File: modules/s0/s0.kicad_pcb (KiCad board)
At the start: 2 copper layers, 54.6 x 86.4 mm, 61 parts, among them J3 USB_C_Receptacle_USB2.0_14P, J4 BAT_JST_01x02, J5 Conn_Coaxial, J6 Conn_Coaxial, Q1 SS8050, Q2 SS8050, Q3 SS8050, SW1 SW_Push, SW2 SW_Push, U1 TXB0108RGY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

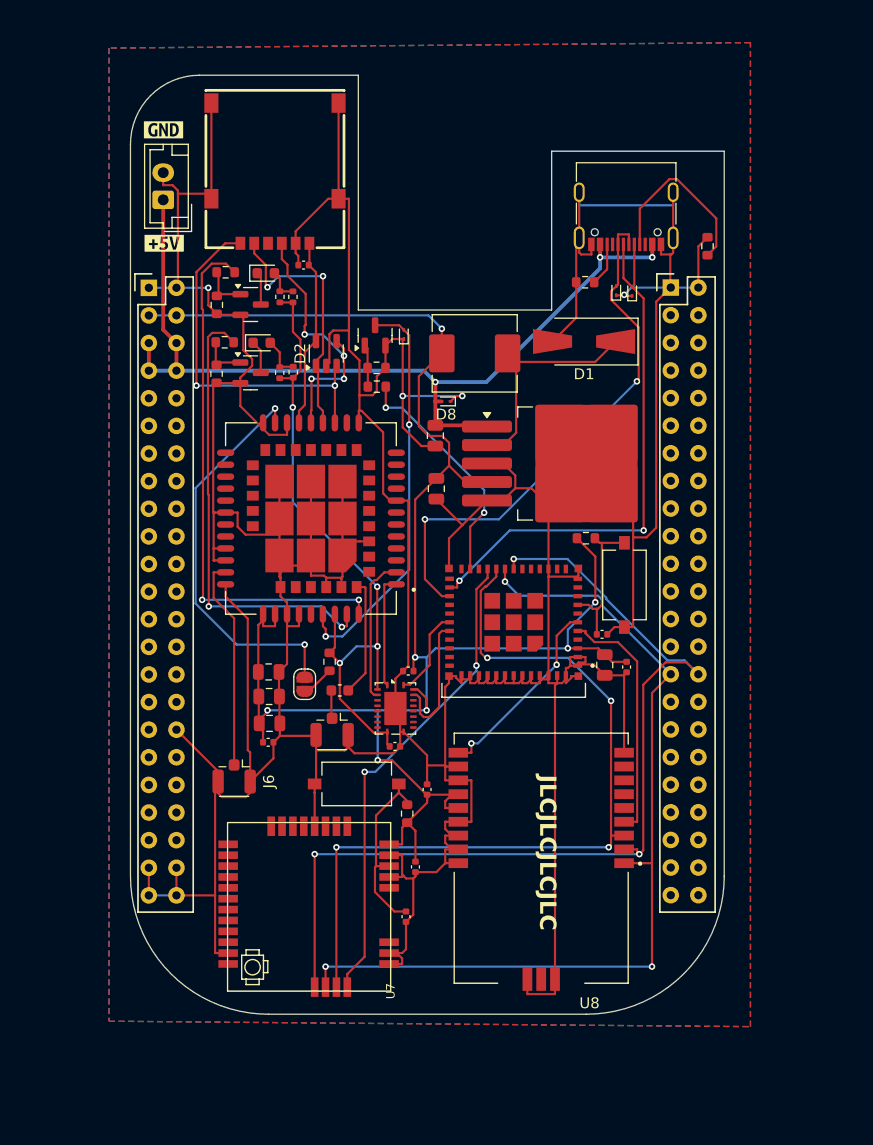
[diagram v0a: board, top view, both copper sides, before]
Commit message: fix: add fuse, ferrite bead and fixes from gpt
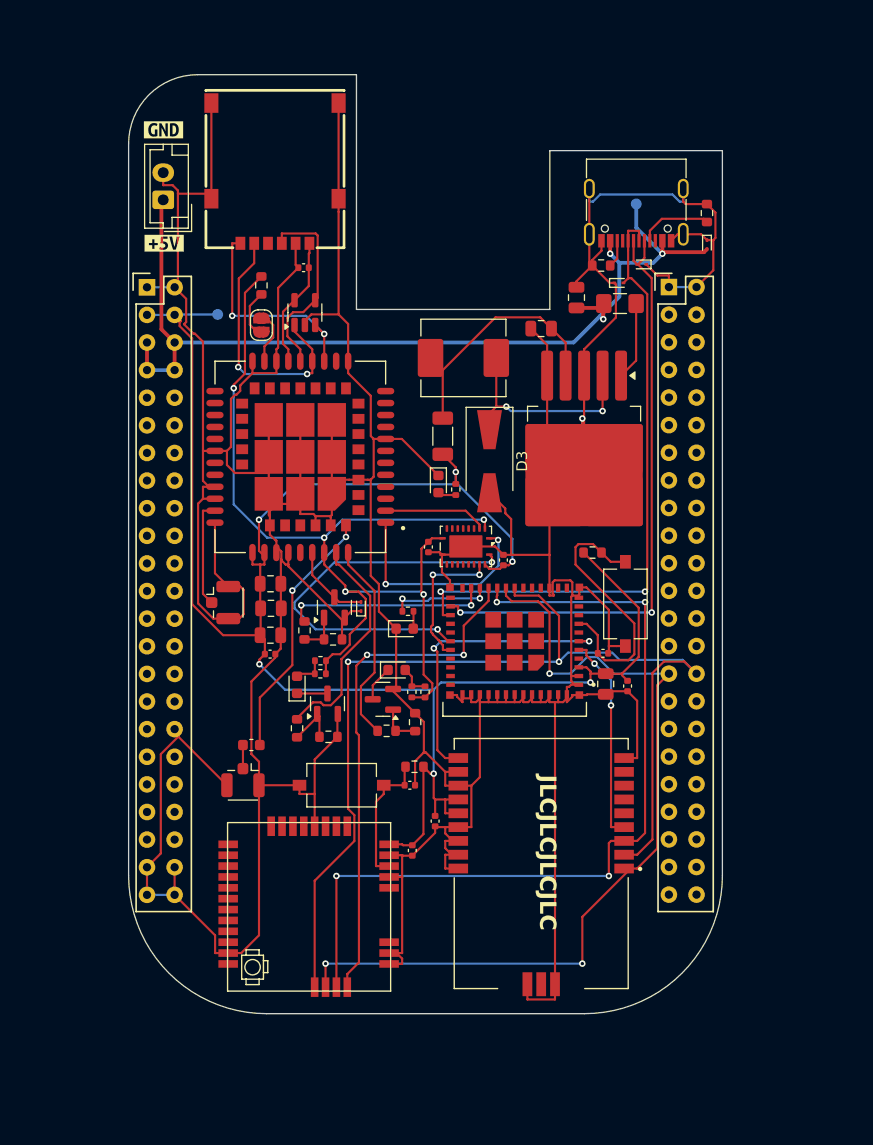
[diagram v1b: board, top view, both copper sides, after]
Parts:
- added D10: LED, LED_SMD:LED_0603_1608Metric, F.Cu at (129.2, 94.9)
- added D9: ESD9B5.0ST5G, Diode_SMD:D_SOD-923, F.Cu at (125.2, 92.9)
- added F1: Fuse, Fuse:Fuse_1206_3216Metric_Pad1.42x1.75mm_HandSolder, F.Cu at (149.0, 65.0)
- added FB1: FerriteBead, Inductor_SMD:L_1206_3216Metric_Pad1.22x1.90mm_HandSolder, F.Cu at (132.7, 77.2)
- added R16: 10K, Resistor_SMD:R_0603_1608Metric, F.Cu at (146.5, 87.9)
- added R17: 10K, Resistor_SMD:R_0603_1608Metric, F.Cu at (130.1, 107.6)
- added TP1: TestPoint, TestPoint:TestPoint_Pad_D1.0mm, B.Cu at (150.5, 55.8)
- added TP2: TestPoint, TestPoint:TestPoint_Pad_D1.0mm, B.Cu at (145.7, 80.9)
- added TP3: TestPoint, TestPoint:TestPoint_Pad_D1.0mm, B.Cu at (112.0, 66.0)
- D1: value 40V 3A 550mV@3A Schottky -> ESD9B5.0ST5G; footprint Diode_SMD:D_SMA-SMB_Universal_Handsoldering -> Diode_SMD:D_SOD-923
- D2: value ESDA6V1SC5 -> ESD9B5.0ST5G; footprint Package_TO_SOT_SMD:SOT-23-5 -> Diode_SMD:D_SOD-923
- D3: value LED -> 40V 3A 550mV@3A Schottky; footprint LED_SMD:LED_0603_1608Metric -> Diode_SMD:D_SMA-SMB_Universal_Handsoldering
- D4: value LED -> ESD9B5.0ST5G; footprint LED_SMD:LED_0603_1608Metric -> Diode_SMD:D_SOD-923
- D5, D7, D8: value ESD9B5.0ST5G -> LED; footprint Diode_SMD:D_SOD-923 -> LED_SMD:LED_0603_1608Metric
- D6: value ESD9B5.0ST5G -> ESDA6V1SC5; footprint Diode_SMD:D_SOD-923 -> Package_TO_SOT_SMD:SOT-23-5
- R10: value 47K -> 100; footprint Resistor_SMD:R_0603_1608Metric -> Resistor_SMD:R_0402_1005Metric
- R12, R8: value 100 -> 47K; footprint Resistor_SMD:R_0402_1005Metric -> Resistor_SMD:R_0603_1608Metric
- R14, R15, R3: value 10K -> 100; footprint Resistor_SMD:R_0603_1608Metric -> Resistor_SMD:R_0402_1005Metric
- R4: value 4.7K -> 10K
- R7: value 47K -> 4.7K
- U1: value TXB0108RGY -> BEAGLEBONEBLACK; footprint Package_DFN_QFN:Texas_RGY_R-PVQFN-N20_EP2.05x3.05mm -> modules:BB_Cape
- U4: value BEAGLEBONEBLACK -> TXB0108RGY; footprint modules:BB_Cape -> Package_DFN_QFN:Texas_RGY_R-PVQFN-N20_EP2.05x3.05mm
- moved D7 47.5 mm to (119.3, 100.1)
- moved R6 42.5 mm to (119.3, 104.1), turned to 90 degrees
- moved R11 41.0 mm to (122.2, 104.8), turned to 180 degrees
- moved Q3 38.3 mm to (127.2, 101.4), turned to 180 degrees
- moved D2 36.4 mm to (157.0, 59.6), turned to -90 degrees
- moved R10 35.0 mm to (131.1, 100.7), turned to -90 degrees
- moved R13 34.9 mm to (121.4, 99.0), turned to 0 degrees
- moved D4 34.6 mm to (151.0, 61.4), turned to 180 degrees
- moved R12 34.1 mm to (130.2, 103.5)
- moved R9 33.6 mm to (121.5, 97.8), turned to 0 degrees
- moved R7 33.4 mm to (127.5, 104.3)
- moved JP1 33.3 mm to (116.0, 67.0)
- moved Q2 31.2 mm to (122.1, 101.8), turned to 90 degrees
- moved D6 28.7 mm to (120.0, 65.8)
- moved R5 27.5 mm to (120.0, 95.1), turned to 90 degrees
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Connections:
- C2 pad 1: +3V3 -> Net-(U2-FB)
- D1 pad 1: Net-(D1-K) -> GND
- D1 pad 2: GND -> USB_D+
- D2 pad 1: SIM_CLK -> GND
- D2 pad 2: GND -> +5V
- D3 pad 2: Net-(D3-A) -> GND
- D4 pad 1: Net-(D4-K) -> GND
- D4 pad 2: Net-(D4-A) -> USB_D-
- D5 pad 2: PWR_KEY -> Net-(D5-A)
- D6 pad 1: GND -> SIM_CLK
- D6 pad 2: USB_D+ -> GND
- D7 pad 1: GND -> Net-(D7-K)
- D7 pad 2: USB_D- -> Net-(D7-A)
- D8 pad 1: GND -> Net-(D8-K)
- D8 pad 2: +5V -> Net-(D8-A)
- L1 pad 1: Net-(D1-K) -> Net-(D3-K)
- L1 pad 2: +3V3 -> Net-(U2-FB)
- Q2 pad 3: Net-(D3-K) -> Net-(D7-K)
- Q3 pad 3: Net-(D4-K) -> Net-(D8-K)
- R10 pad 1: GND -> Net-(D8-A)
- R10 pad 2: Net-(Q2-B) -> +1V8
- R11 pad 2: Net-(Q3-B) -> Net-(Q2-B)
- R12 pad 1: Net-(D3-A) -> GND
- R12 pad 2: +1V8 -> Net-(Q3-B)
- R13 pad 1: Net-(D4-A) -> Net-(D7-A)
- R14 pad 1: +3V3 -> Net-(D8-A)
- R14 pad 2: MCU_RST -> +1V8
- R15 pad 1: +3V3 -> Net-(D10-A)
- R15 pad 2: LORA_RST -> LED
- R3 pad 1: +1V8 -> Net-(D5-A)
- R3 pad 2: Net-(JP1-A) -> +3V3
- R4 pad 1: Net-(Q1-B) -> +1V8
- R4 pad 2: SIM7080G_PWR -> Net-(JP1-A)
- R5 pad 1: Net-(Q2-B) -> Net-(Q1-B)
- R5 pad 2: NETLIGHT -> SIM7080G_PWR
- R6 pad 1: Net-(Q3-B) -> Net-(Q2-B)
- R6 pad 2: STATUS -> NETLIGHT
- R7 pad 1: GND -> Net-(Q3-B)
- R7 pad 2: Net-(Q1-B) -> STATUS
- R8 pad 1: Net-(D3-A) -> GND
- R8 pad 2: +1V8 -> Net-(Q1-B)
- R9 pad 1: Net-(D4-A) -> Net-(D7-A)
- U2 pad 1: +5V -> Net-(U2-VIN)
- U2 pad 2: Net-(D1-K) -> Net-(D3-K)
- U2 pad 4: +3V3 -> Net-(U2-FB)
- U6 pad 22: unconnected-(U6-IO8-Pad22) -> LED
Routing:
- net Net-(JP1-B): track 36.9 -> 5.02 mm, vias 2 -> 0
- net STATUS: track 49.5 -> 18.6 mm, vias 2 -> 0
- net PWR_KEY: track 37.5 -> 7.58 mm, vias 2 -> 0
- net SIM7080G_TXD: track 8.27 -> 36.7 mm, vias 0 -> 2
- net +1V8: track 61.4 -> 89.8 mm, vias 4 -> 5
- net Net-(U2-FB): track 0.00 -> 23.3 mm
- net NETLIGHT: track 42.3 -> 20.9 mm, vias 2 -> 0
- net Net-(D1-K): track 20.7 -> 0.00 mm
- net Net-(D3-K): track 3.05 -> 20.1 mm, vias 0 -> 2
- net SIM_DATA: track 33.6 -> 20.3 mm
- net GNSS_ANT: track 10.9 -> 23.5 mm, vias 0 -> 2
- net MCU_RST: track 13.5 -> 25.2 mm
- net Net-(J3-CC1): track 16.7 -> 6.75 mm
- net MOSI: track 88.3 -> 98.1 mm, vias 3 -> 2
- net RF_ANT: track 19.6 -> 9.88 mm
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- removed copper zone on B.Cu, net GND
- removed copper zone on F.Cu, net GND
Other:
- outline, holes or cut-outs redrawn
- board text added: "https://abstractmachines.fr"
- board text removed: "https://github.com/absmach/s0"

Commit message: fix: add logo name of the board on silkscreen
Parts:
- moved G*** 3.14 mm to (131.5, 109.5)
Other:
- board text added: "S0 IoT Gateway"
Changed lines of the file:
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@@
 	(footprint "LOGO"
 		(layer "B.Cu")
-		(at 132 112.6 180)
+		(at 131.5 109.5 180)
 		(property "Reference" "G***"
 			(at 0 0 0)
@@
 		)
 	)
-	(gr_text "https://abstractmachines.fr"
-		(at 147.4 128.1 0)
+	(gr_text "S0 IoT Gateway"
+		(at 139.763616 128 0)
 		(layer "B.SilkS")
 		(effects
+			(font
+				(size 1.5 1.5)
+				(thickness 0.2)
+			)
+			(justify left bottom mirror)
+		)
+	)
+	(gr_text "https://abstractmachines.fr"
+		(at 146.942189 124.772838 0)
+		(layer "B.SilkS")
+		(effects

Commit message: fix(silkscreen): Add logo and website name
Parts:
- moved G*** 22.4 mm to (130.3, 87.1)
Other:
- board text added: "."
- board text added: "IoT Gateway"
- board text added: "S0"
- board text added: "www.absmach.eu"
- board text removed: "S0 IoT Gateway"
- board text removed: "https://abstractmachines.fr"

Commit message: style: add new aligned logo
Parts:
- removed the G*** at (130.3, 87.1)
- added G***: LOGO, LOGO, F.Cu at (107.9, 123.6)
- added G***: LOGO, LOGO, B.Cu at (130.9, 106.9)
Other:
- board text removed: "."
- board text removed: "IoT Gateway"
- board text removed: "www.absmach.eu"

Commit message: chore: finalize production files for s0
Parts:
- removed G***: LOGO, LOGO
- added G1: LOGO, LOGO, F.Cu at (108.7, 123.4)
- C1: value 100uF -> 10uF
- C16: value 100uF -> 0.1uF
- moved C12 0.58 mm to (138.7, 89.0), turned to 0 degrees
- renumbered G*** to G2
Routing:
- net SIM7080G_TXD: track 36.7 -> 10.1 mm
- net GND: track 610.6 -> 623.9 mm
- net MCU_RST: track 25.2 -> 14.0 mm
- net LED: track 9.42 -> 17.3 mm
- net SCK: track 78.2 -> 70.4 mm
- net UART1_TXD: track 20.0 -> 12.2 mm
- net +1V8: track 89.8 -> 85.7 mm, vias 5 -> 7
- net GNSS_ANT: track 23.5 -> 27.3 mm
- net SIM_DATA: track 20.3 -> 17.1 mm
- net USB_D+: track 58.5 -> 56.0 mm
- net SIM7080G_RXD: track 13.4 -> 11.0 mm
- net RC_CS: track 19.1 -> 21.4 mm, vias 2 -> 0
- net SIM_CLK: track 24.2 -> 25.3 mm
- net RC_SDN: track 27.2 -> 26.1 mm
- net LORA_CS: track 47.5 -> 46.6 mm
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- added copper zone on B.Cu, net GND
- added copper zone on F.Cu, net GND

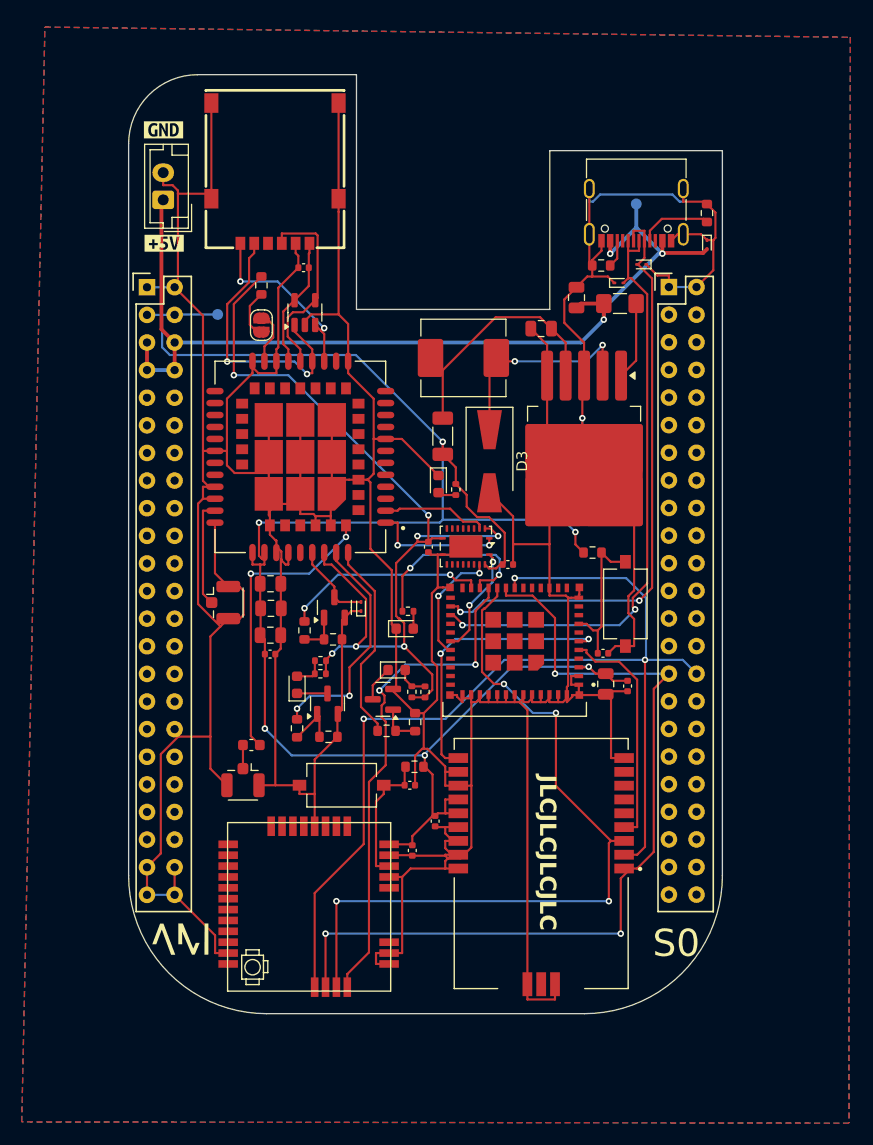
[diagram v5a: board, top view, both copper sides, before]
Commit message: fix: route PCB
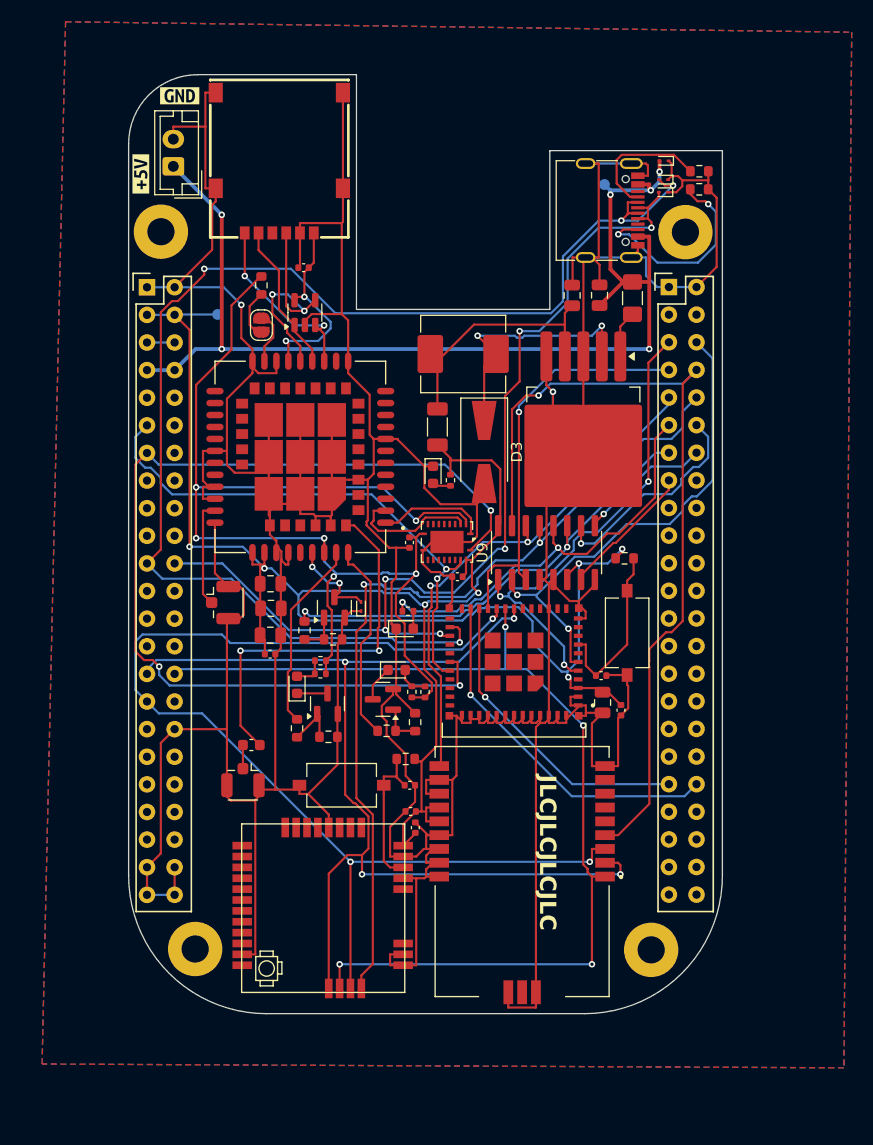
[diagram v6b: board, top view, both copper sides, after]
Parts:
- removed G1: LOGO, LOGO
- added REF1: MountingHole_2.5mm_Pad, MountingHole:MountingHole_2.5mm_Pad, F.Cu at (106.8, 58.4)
- added REF2: MountingHole_2.5mm_Pad, MountingHole:MountingHole_2.5mm_Pad, F.Cu at (155.0, 58.4)
- added REF3: MountingHole_2.5mm_Pad, MountingHole:MountingHole_2.5mm_Pad, F.Cu at (109.9, 124.4)
- added REF4: MountingHole_2.5mm_Pad, MountingHole:MountingHole_2.5mm_Pad, F.Cu at (151.9, 124.4)
- added U9: 74HC138, Package_SO:SOIC-16_3.9x9.9mm_P1.27mm, F.Cu at (142.2, 87.9)
- moved R1 11.4 mm to (156.3, 54.5), turned to 180 degrees
- moved D1 9.29 mm to (153.0, 54.8), turned to 180 degrees
- moved D2 8.66 mm to (153.1, 51.9), turned to 180 degrees
- moved D4 8.05 mm to (153.0, 53.6)
- moved kibuzzard-67D322D0 6.72 mm to (104.9, 53.1), turned to 90 degrees
- moved C12 4.77 mm to (134.1, 90.1), turned to 180 degrees
- moved C2 4.17 mm to (144.6, 64.2), turned to 90 degrees
- moved R2 3.91 mm to (156.3, 52.8), turned to 180 degrees
- moved J3 3.70 mm to (146.9, 56.4), turned to -90 degrees
- moved kibuzzard-67D322D7 3.47 mm to (108.5, 45.9)
- moved TP1 3.43 mm to (147.6, 54.0)
- moved J4 3.22 mm to (107.9, 52.4)
- moved R16 3.00 mm to (149.4, 88.4)
- moved SW1 2.66 mm to (149.7, 95.3)
- moved C18 2.42 mm to (129.8, 111.7), turned to 180 degrees
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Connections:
- U1 pad P8_10: unconnected-(U1-TIMER6-PadP8_10) -> LORA_CS
- U1 pad P8_11: unconnected-(U1-GPIO1_13-PadP8_11) -> LED
- U1 pad P8_12: unconnected-(U1-GPIO1_12-PadP8_12) -> EXT_GPIO1
- U1 pad P8_13: unconnected-(U1-EHRPWM2B-PadP8_13) -> SIM7080G_PWR
- U1 pad P8_14: unconnected-(U1-GPIO0_26-PadP8_14) -> EXT_GPIO2
- U1 pad P8_15: unconnected-(U1-GPIO1_15-PadP8_15) -> EXT_GPIO3
- U1 pad P8_29: MISO -> unconnected-(U1-GPIO2_23-PadP8_29)
- U1 pad P8_30: MOSI -> unconnected-(U1-GPIO2_25-PadP8_30)
- U1 pad P8_31: SCLK -> unconnected-(U1-UART5_CTSN-PadP8_31)
- U1 pad P8_32: CS -> unconnected-(U1-UART5_RTSN-PadP8_32)
- U1 pad P8_33: INT -> unconnected-(U1-UART4_RTSN-PadP8_33)
- U1 pad P8_34: RST -> unconnected-(U1-UART3_RTSN-PadP8_34)
- U1 pad P8_37: unconnected-(U1-UART5_TXD-PadP8_37) -> MBUS_RX
- U1 pad P8_38: unconnected-(U1-UART5_RXD-PadP8_38) -> MBUS_TX
- U1 pad P8_5: unconnected-(U1-GPIO1_2-PadP8_5) -> MUX1
- U1 pad P8_6: unconnected-(U1-GPIO1_3-PadP8_6) -> MUX2
- U1 pad P8_7: unconnected-(U1-TIMER4-PadP8_7) -> MUX3
- U1 pad P8_8: unconnected-(U1-TIMER7-PadP8_8) -> WMBUS_CS
- U1 pad P8_9: unconnected-(U1-TIMER5-PadP8_9) -> WMBUS_SDN
- U1 pad P9_11: unconnected-(U1-UART4_RXD-PadP9_11) -> SIM7080G_RXD
- U1 pad P9_13: unconnected-(U1-UART4_TXD-PadP9_13) -> SIM7080G_TXD
- U1 pad P9_21: unconnected-(U1-UART2_TXD-PadP9_21) -> USB_D-
- U1 pad P9_22: unconnected-(U1-UART2_RXD-PadP9_22) -> USB_D+
- U1 pad P9_29: unconnected-(U1-SPI1_D0-PadP9_29) -> MOSI
- U1 pad P9_30: unconnected-(U1-SPI1_D1-PadP9_30) -> MISO
- U1 pad P9_31: unconnected-(U1-SPI1_SCLK-PadP9_31) -> SCK
- U1 pad P9_5: +5V -> Net-(U1-VDD_5V-PadP9_5)
- U1 pad P9_6: +5V -> Net-(U1-VDD_5V-PadP9_5)
- U4 pad 16: SIM7080G_SDA -> unconnected-(U4-B4-Pad16)
- U4 pad 17: SIM7080G_SCL -> unconnected-(U4-B3-Pad17)
- U4 pad 4: SCL_1v8 -> unconnected-(U4-A3-Pad4)
- U4 pad 5: SDA_1v8 -> unconnected-(U4-A4-Pad5)
- U6 pad 21: LORA_CS -> MUX3
- U6 pad 22: LED -> MBUS_RX
- U6 pad 23: SIM7080G_PWR -> MBUS_TX
- U6 pad 5: RC_CS -> MUX1
- U6 pad 6: RC_SDN -> MUX2
- U8 pad 10: RC_SDN -> WMBUS_SDN
- U8 pad 4: RC_CS -> WMBUS_CS
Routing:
- net SIM7080G_TXD: track 10.1 -> 91.5 mm, vias 2 -> 3
- net WMBUS_CS: track 0.00 -> 76.5 mm, vias 0 -> 1
- net USB_D-: track 55.5 -> 120.9 mm, vias 2 -> 4
- net WMBUS_SDN: track 0.00 -> 48.3 mm, vias 0 -> 2
- net MUX2: track 0.00 -> 45.7 mm, vias 0 -> 2
- net MUX1: track 0.00 -> 44.1 mm, vias 0 -> 3
- net SIM7080G_RXD: track 11.0 -> 49.3 mm
- net MUX3: track 0.00 -> 37.9 mm, vias 0 -> 1
- net USB_D+: track 56.0 -> 90.6 mm, vias 2 -> 6
- net LORA_CS: track 46.6 -> 80.3 mm
- net MBUS_TX: track 0.00 -> 33.0 mm, vias 0 -> 1
- net SCK: track 70.4 -> 102.9 mm, vias 4 -> 3
- net MBUS_RX: track 0.00 -> 28.6 mm, vias 0 -> 1
- net RC_SDN: track 26.1 -> 0.00 mm, vias 2 -> 0
- net SIM7080G_PWR: track 18.7 -> 43.1 mm
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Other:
- board text removed: "S0"

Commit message: USB-C modification
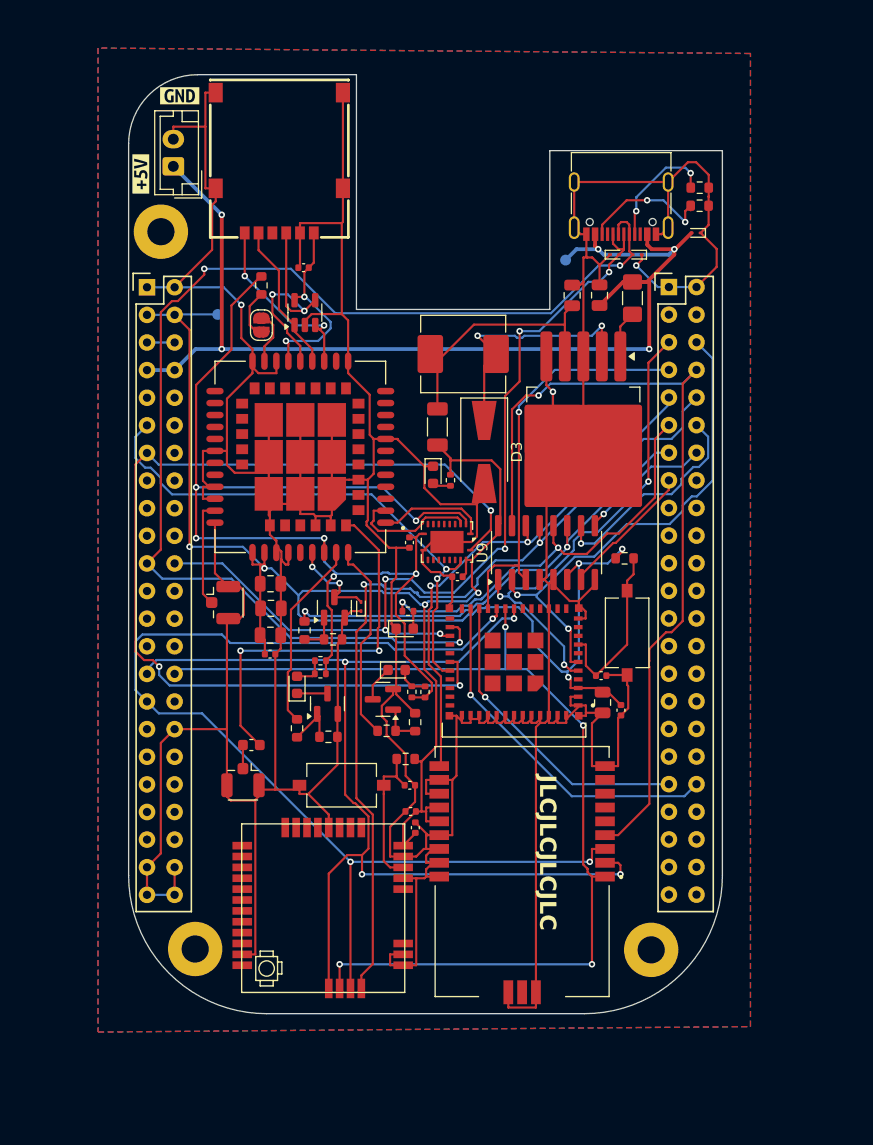
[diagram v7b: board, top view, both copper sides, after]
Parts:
- removed REF2: MountingHole_2.5mm_Pad, MountingHole:MountingHole_2.5mm_Pad
- moved TP1 7.81 mm to (144.0, 61.0)
- moved D4 7.32 mm to (150.6, 60.5)
- moved D1 7.29 mm to (148.5, 60.5), turned to 0 degrees
- moved D2 7.25 mm to (156.0, 58.5)
- moved J3 2.68 mm to (149.1, 54.9), turned to 180 degrees
- moved R2 1.51 mm to (156.3, 54.3)
- moved R1 1.51 mm to (156.3, 56.0)
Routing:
- net USB_D-: track 120.9 -> 111.8 mm, vias 4 -> 3
- net USB_D+: track 90.6 -> 83.1 mm
- net Net-(J3-CC2): track 19.2 -> 12.4 mm
- net GND: track 625.0 -> 619.4 mm, vias 2 -> 3
- net Net-(J3-CC1): track 12.2 -> 11.1 mm, vias 0 -> 2
- net +5V: track 100.6 -> 100.8 mm, vias 6 -> 5
